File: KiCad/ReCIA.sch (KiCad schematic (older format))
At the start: 1 part, among them U1 8520_DIP

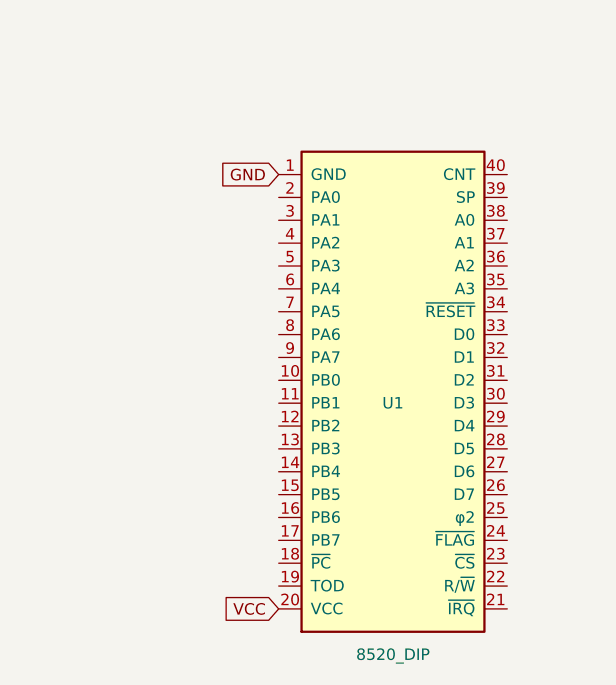
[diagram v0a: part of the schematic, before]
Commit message: Add nets
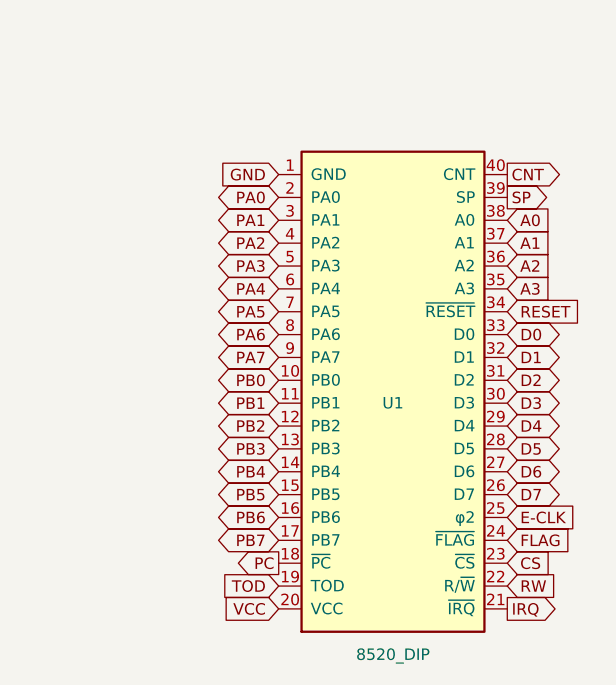
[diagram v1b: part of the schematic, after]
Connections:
- net PB0: now reaches U1.10 (PB0)
- net PB1: now reaches U1.11 (PB1)
- net PB2: now reaches U1.12 (PB2)
- net PB3: now reaches U1.13 (PB3)
- net PB4: now reaches U1.14 (PB4)
- net PB5: now reaches U1.15 (PB5)
- net PB6: now reaches U1.16 (PB6)
- net PB7: now reaches U1.17 (PB7)
- net PC: now reaches U1.18 (~PC)
- net TOD: now reaches U1.19 (TOD)
- net PA0: now reaches U1.2 (PA0)
- net IRQ: now reaches U1.21 (~IRQ)
- net RW: now reaches U1.22 (R/~W)
- net CS: now reaches U1.23 (~CS)
- net FLAG: now reaches U1.24 (~FLAG)
- net E-CLK: now reaches U1.25 (φ2)
- net D7: now reaches U1.26 (D7)
- net D6: now reaches U1.27 (D6)
- net D5: now reaches U1.28 (D5)
- net D4: now reaches U1.29 (D4)
- net PA1: now reaches U1.3 (PA1)
- net D3: now reaches U1.30 (D3)
- net D2: now reaches U1.31 (D2)
- net D1: now reaches U1.32 (D1)
- net D0: now reaches U1.33 (D0)
- net RESET: now reaches U1.34 (~RESET)
- net A3: now reaches U1.35 (A3)
- net A2: now reaches U1.36 (A2)
- net A1: now reaches U1.37 (A1)
- net A0: now reaches U1.38 (A0)
- net SP: now reaches U1.39 (SP)
- net PA2: now reaches U1.4 (PA2)
- net CNT: now reaches U1.40 (CNT)
- net PA3: now reaches U1.5 (PA3)
- net PA4: now reaches U1.6 (PA4)
- net PA5: now reaches U1.7 (PA5)
- net PA6: now reaches U1.8 (PA6)
- net PA7: now reaches U1.9 (PA7)
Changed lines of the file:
@@
 GND
 $Comp
-L power:VCC #PWR?
+L power:VCC #PWR0101
 U 1 1 66BFF4F3
 P 1050 1100
-F 0 "#PWR?" H 1065 1273 50  0001 C CNN
+F 0 "#PWR0101" H 1065 1273 50  0001 C CNN
 F 1 "VCC" H 1065 1273 50  0001 C CNN
 F 2 "" H 1050 1100 50  0001 C CNN
@@
 $EndComp
 $Comp
-L power:PWR_FLAG #FLG?
+L power:PWR_FLAG #FLG0101
 U 1 1 66BFFF76
 P 1050 1200
-F 0 "#FLG?" H 1050 1275 50  0001 C CNN
+F 0 "#FLG0101" H 1050 1275 50  0001 C CNN
 F 1 "PWR_FLAG" H 1050 1373 50  0001 C CNN
 F 2 "" H 1050 1200 50  0001 C CNN
@@
 VCC
 $Comp
-L power:PWR_FLAG #FLG?
+L power:PWR_FLAG #FLG0102
 U 1 1 66C0324F
 P 1200 1100
-F 0 "#FLG?" H 1200 1175 50  0001 C CNN
+F 0 "#FLG0102" H 1200 1175 50  0001 C CNN
 F 1 "PWR_FLAG" H 1200 1273 50  0001 C CNN
 F 2 "" H 1200 1100 50  0001 C CNN
@@
 $EndComp
 $Comp
-L power:GND #PWR?
+L power:GND #PWR0102
 U 1 1 66C03B19
 P 1200 1200
-F 0 "#PWR?" H 1200 950 50  0001 C CNN
+F 0 "#PWR0102" H 1200 950 50  0001 C CNN
 F 1 "GND" H 1205 1027 50  0001 C CNN
 F 2 "" H 1200 1200 50  0001 C CNN
@@
 Wire Wire Line
 	1200 1150 1200 1200
+Text GLabel 2250 2500 0    50   BiDi ~ 0
+PA0
+Text GLabel 2250 2600 0    50   BiDi ~ 0
+PA1
+Text GLabel 2250 2700 0    50   BiDi ~ 0
+PA2
+Text GLabel 2250 2800 0    50   BiDi ~ 0
+PA3
+Text GLabel 2250 2900 0    50   BiDi ~ 0
+PA4
+Text GLabel 2250 3000 0    50   BiDi ~ 0
+PA5
+Text GLabel 2250 3100 0    50   BiDi ~ 0
+PA6
+Text GLabel 2250 3200 0    50   BiDi ~ 0
+PA7
+Text GLabel 2250 3300 0    50   BiDi ~ 0
+PB0
+Text GLabel 2250 3400 0    50   BiDi ~ 0
+PB1
+Text GLabel 2250 3500 0    50   BiDi ~ 0
+PB2
+Text GLabel 2250 3600 0    50   BiDi ~ 0
+PB3
+Text GLabel 2250 3700 0    50   BiDi ~ 0
+PB4
+Text GLabel 2250 3800 0    50   BiDi ~ 0
+PB5
+Text GLabel 2250 3900 0    50   BiDi ~ 0
+PB6
+Text GLabel 2250 4000 0    50   BiDi ~ 0
+PB7
+Text GLabel 3250 2600 2    50   Input ~ 0
+A0
+Text GLabel 3250 2700 2    50   Input ~ 0
+A1
+Text GLabel 3250 2800 2    50   Input ~ 0
+A2
+Text GLabel 3250 2900 2    50   Input ~ 0
+A3
+Text GLabel 3250 3000 2    50   Input ~ 0
+RESET
+Text GLabel 3250 3100 2    50   BiDi ~ 0
+D0
+Text GLabel 3250 3200 2    50   BiDi ~ 0
+D1
+Text GLabel 3250 3300 2    50   BiDi ~ 0
+D2
+Text GLabel 3250 3400 2    50   BiDi ~ 0
+D3
+Text GLabel 3250 3500 2    50   BiDi ~ 0
+D4
+Text GLabel 3250 3600 2    50   BiDi ~ 0
+D5
+Text GLabel 3250 3700 2    50   BiDi ~ 0
+D6
+Text GLabel 3250 3800 2    50   BiDi ~ 0
+D7
+Text GLabel 3250 3900 2    50   Input ~ 0
+E-CLK
+Text GLabel 2250 4100 0    50   Output ~ 0
+PC
+Text GLabel 2250 4200 0    50   Input ~ 0
+TOD
+Text GLabel 3250 4000 2    50   Input ~ 0
+FLAG
+Text GLabel 3250 4100 2    50   Input ~ 0
+CS
+Text GLabel 3250 4200 2    50   Input ~ 0
+RW
+Text GLabel 3250 4300 2    50   Output ~ 0
+IRQ
+Text GLabel 3250 2400 2    50   Output ~ 0
+CNT
+Text GLabel 3250 2500 2    50   Output ~ 0
+SP
 $EndSCHEMATC

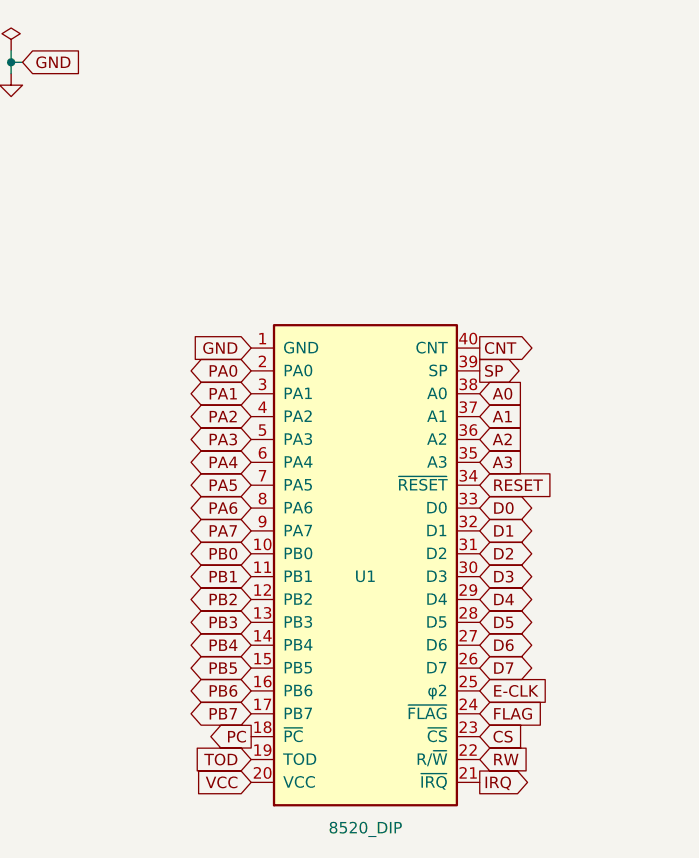
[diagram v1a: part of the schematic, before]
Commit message: Added a 3.3V LDO Voltage Regulator
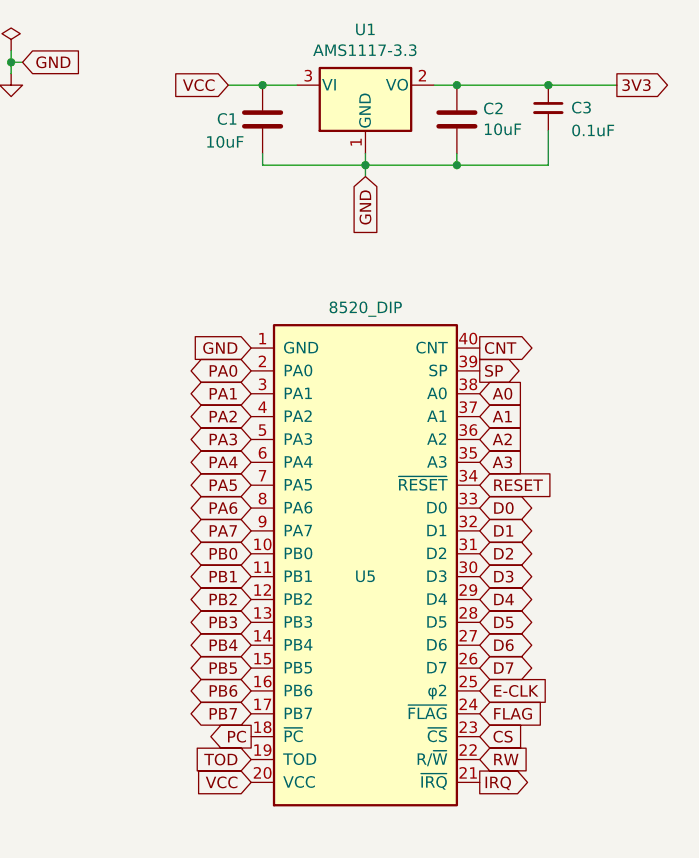
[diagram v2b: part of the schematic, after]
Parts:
- removed U1: 8520_DIP, Package_DIP:DIP-40_W15.24mm, symbol ReCIA:8520_DIP
- added C1, C2: 10uF, Capacitor_SMD:C_1206_3216Metric_Pad1.33x1.80mm_HandSolder, symbol Device:C
- added C3: 0.1uF, Capacitor_SMD:C_0805_2012Metric_Pad1.18x1.45mm_HandSolder, symbol Device:C_Small
- added U1: AMS1117-3.3, Package_TO_SOT_SMD:SOT-223-3_TabPin2, symbol Regulator_Linear:AMS1117-3.3
- added U5: 8520_DIP, Package_DIP:DIP-40_W15.24mm, symbol ReCIA:8520_DIP
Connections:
- net A0: now also U5.38 (A0)
- net A1: now also U5.37 (A1)
- net A2: now also U5.36 (A2)
- net A3: now also U5.35 (A3)
- net CNT: now also U5.40 (CNT)
- net CS: now also U5.23 (~CS)
- net D0: now also U5.33 (D0)
- net D1: now also U5.32 (D1)
- net D2: now also U5.31 (D2)
- net D3: now also U5.30 (D3)
- net D4: now also U5.29 (D4)
- net D5: now also U5.28 (D5)
- net D6: now also U5.27 (D6)
- net D7: now also U5.26 (D7)
- net E-CLK: now also U5.25 (φ2)
- net FLAG: now also U5.24 (~FLAG)
- net GND: now also C1.2, C2.2, C3.2, U1.1 (GND), U5.1 (GND)
- net IRQ: now also U5.21 (~IRQ)
- net PA0: now also U5.2 (PA0)
- net PA1: now also U5.3 (PA1)
- net PA2: now also U5.4 (PA2)
- net PA3: now also U5.5 (PA3)
- net PA4: now also U5.6 (PA4)
- net PA5: now also U5.7 (PA5)
- net PA6: now also U5.8 (PA6)
- net PA7: now also U5.9 (PA7)
- net PB0: now also U5.10 (PB0)
- net PB1: now also U5.11 (PB1)
- net PB2: now also U5.12 (PB2)
- net PB3: now also U5.13 (PB3)
- net PB4: now also U5.14 (PB4)
- net PB5: now also U5.15 (PB5)
- net PB6: now also U5.16 (PB6)
- net PB7: now also U5.17 (PB7)
- net PC: now also U5.18 (~PC)
- net RESET: now also U5.34 (~RESET)
- net RW: now also U5.22 (R/~W)
- net SP: now also U5.39 (SP)
- net TOD: now also U5.19 (TOD)
- net VCC: now also C1.1, U1.3 (VI), U5.20 (VCC)
- new net 3V3: C2.1, C3.1, U1.2 (VO)
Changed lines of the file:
@@
 Comment4 ""
 $EndDescr
-$Comp
-L ReCIA:8520_DIP U1
-U 1 1 66BF3B9F
-P 2750 3400
-F 0 "U1" H 2750 3400 50  0000 C CNN
-F 1 "8520_DIP" H 2750 2300 50  0000 C CNN
-F 2 "Package_DIP:DIP-40_W15.24mm" H 2800 2050 50  0001 L CNN
-F 3 "" H 2750 3400 50  0001 C CNN
-	1    2750 3400
-	1    0    0    -1
-$EndComp
 Text GLabel 2250 2400 0    50   Input ~ 0
 GND
@@
 Text GLabel 3250 2500 2    50   Output ~ 0
 SP
+$Comp
+L ReCIA:8520_DIP U5
+U 1 1 66C0FD06
+P 2750 3400
+F 0 "U5" H 2750 3400 50  0000 C CNN
+F 1 "8520_DIP" H 2750 4576 50  0000 C CNN
+F 2 "Package_DIP:DIP-40_W15.24mm" H 2200 2300 50  0001 L CNN
+F 3 "" H 2750 3200 50  0001 C CNN
+	1    2750 3400
+	1    0    0    -1
+$EndComp
+$Comp
+L Regulator_Linear:AMS1117-3.3 U1
+U 1 1 66C15FFE
+P 2750 1250
+F 0 "U1" H 2750 1492 50  0000 C CNN
+F 1 "AMS1117-3.3" H 2750 1401 50  0000 C CNN
+F 2 "Package_TO_SOT_SMD:SOT-223-3_TabPin2" H 2750 1450 50  0001 C CNN
+F 3 "http://www.advanced-monolithic.com/pdf/ds1117.pdf" H 2850 1000 50  0001 C CNN
+	1    2750 1250
+	1    0    0    -1
+$EndComp
+Text GLabel 2750 1650 3    50   Input ~ 0
+GND
+Text GLabel 2150 1250 0    50   Input ~ 0
+VCC
+Text GLabel 3850 1250 2    50   Output ~ 0
+3V3
+Wire Wire Line
+	2150 1250 2300 1250
+Wire Wire Line
+	3050 1250 3150 1250
+$Comp
+L Device:C C1
+U 1 1 66C1D6E1
+P 2300 1400
+F 0 "C1" H 2100 1400 50  0000 L CNN
+F 1 "10uF" H 2050 1300 50  0000 L CNN
+F 2 "Capacitor_SMD:C_1206_3216Metric_Pad1.33x1.80mm_HandSolder" H 2338 1250 50  0001 C CNN
+F 3 "~" H 2300 1400 50  0001 C CNN
+	1    2300 1400
+	1    0    0    -1
+$EndComp
+Connection ~ 2300 1250
+Wire Wire Line
+	2300 1250 2450 1250
+Wire Wire Line
+	2300 1550 2300 1600
+Wire Wire Line
+	2300 1600 2750 1600
+Wire Wire Line
+	2750 1600 2750 1550
+Wire Wire Line
+	2750 1650 2750 1600
+Connection ~ 2750 1600
+$Comp
+L Device:C C2
+U 1 1 66C1E80A
+P 3150 1400
+F 0 "C2" H 3265 1446 50  0000 L CNN
+F 1 "10uF" H 3265 1355 50  0000 L CNN
+F 2 "Capacitor_SMD:C_1206_3216Metric_Pad1.33x1.80mm_HandSolder" H 3188 1250 50  0001 C CNN
+F 3 "~" H 3150 1400 50  0001 C CNN
+	1    3150 1400
+	1    0    0    -1
+$EndComp
+Connection ~ 3150 1250
+Wire Wire Line
+	2750 1600 3150 1600
+Wire Wire Line
+	3150 1600 3150 1550
+$Comp
+L Device:C_Small C3
+U 1 1 66C24424
+P 3550 1350
+F 0 "C3" H 3650 1350 50  0000 L CNN
+F 1 "0.1uF" H 3650 1250 50  0000 L CNN
+F 2 "Capacitor_SMD:C_0805_2012Metric_Pad1.18x1.45mm_HandSolder" H 3550 1350 50  0001 C CNN
+F 3 "~" H 3550 1350 50  0001 C CNN
+	1    3550 1350
+	1    0    0    -1
+$EndComp
+Wire Wire Line
+	3150 1250 3550 1250
+Wire Wire Line
+	3550 1250 3850 1250
+Connection ~ 3550 1250
+Wire Wire Line
+	3150 1600 3550 1600
+Wire Wire Line
+	3550 1600 3550 1450
+Connection ~ 3150 1600
 $EndSCHEMATC

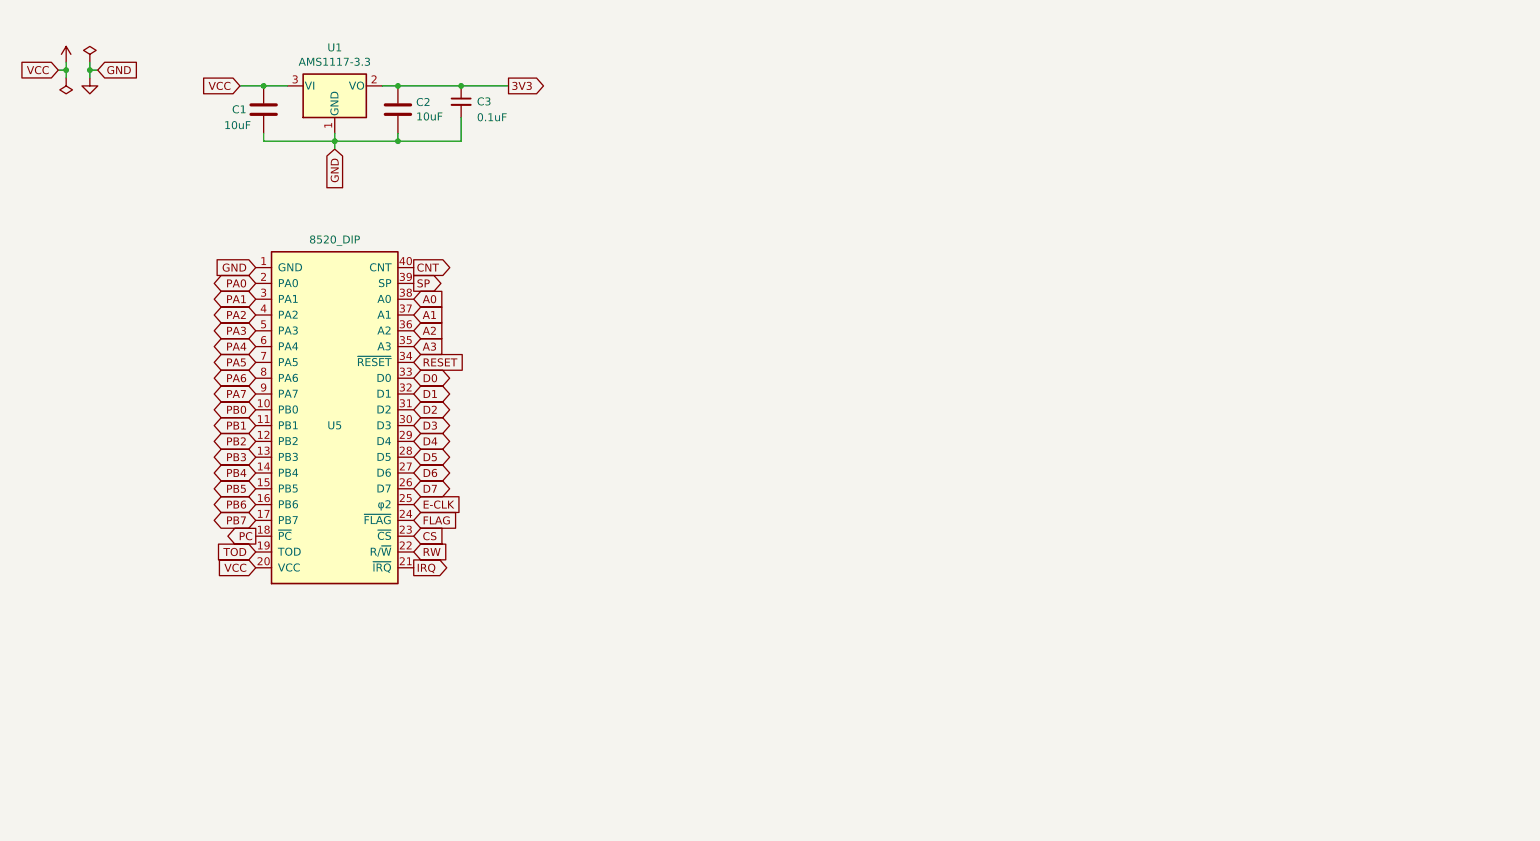
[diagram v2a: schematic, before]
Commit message: Add 10 Max FPGA
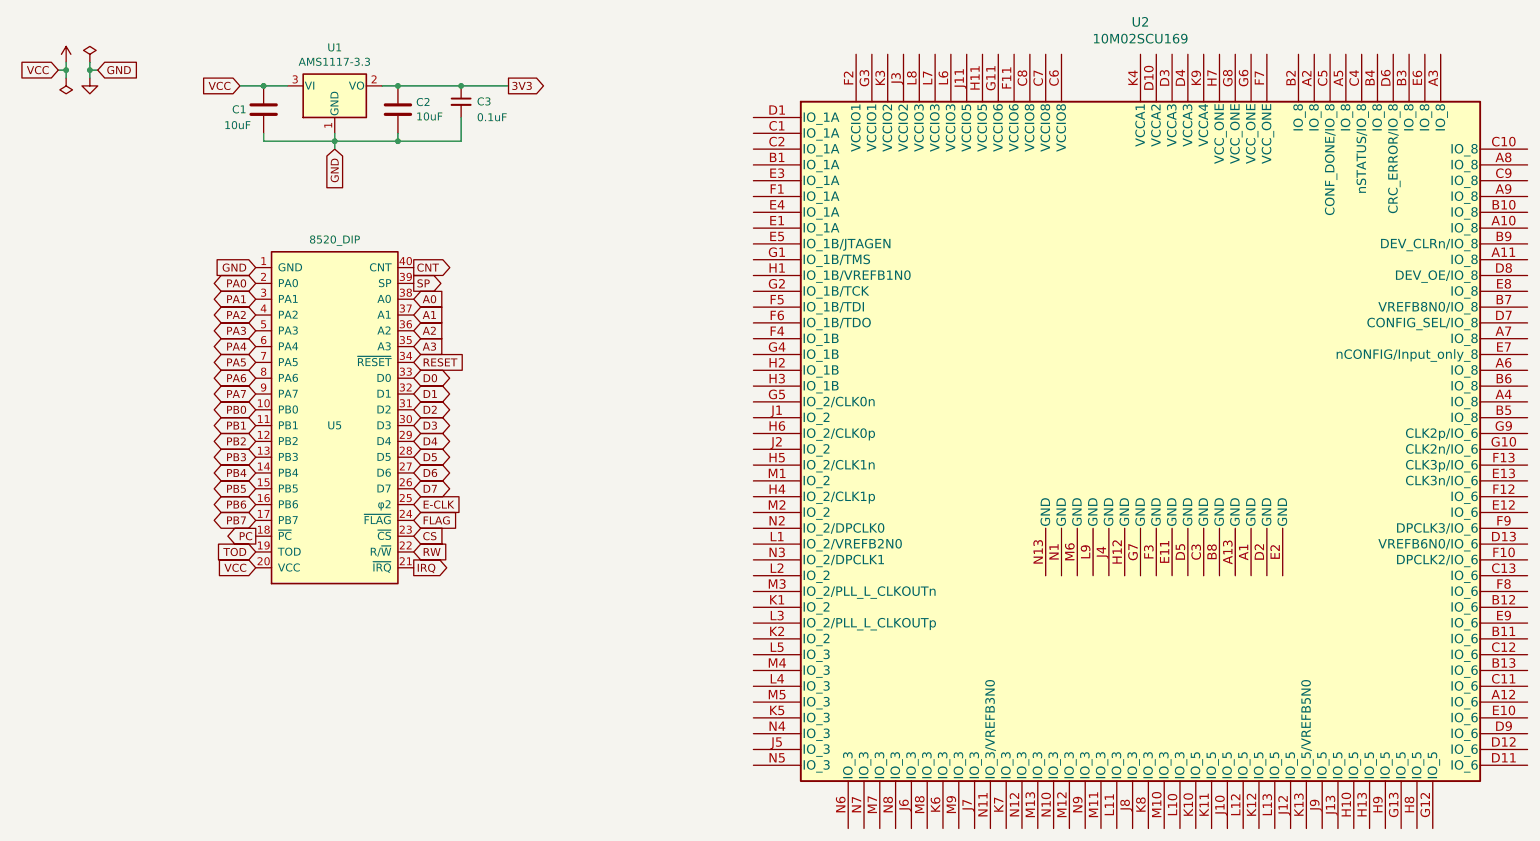
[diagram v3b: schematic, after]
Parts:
- added U2: 10M02SCU169, ReCIA:BGA-169_11.0x11.0mm_Layout13x13_P0.8mm_Ball0.5mm_Pad0.35mm_NSMD, symbol ReCIA:10M02SCU169
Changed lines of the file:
@@
 	3550 1600 3550 1450
 Connection ~ 3150 1600
+$Comp
+L ReCIA:10M02SCU169 U2
+U 1 1 66C35F6F
+P 7850 3500
+F 0 "U2" H 7850 6153 60  0000 C CNN
+F 1 "10M02SCU169" H 7850 6047 60  0000 C CNN
+F 2 "ReCIA:BGA-169_11.0x11.0mm_Layout13x13_P0.8mm_Ball0.5mm_Pad0.35mm_NSMD" H 7850 3850 60  0001 C CNN
+F 3 "" H 9300 4700 60  0000 C CNN
+	1    7850 3500
+	1    0    0    -1
+$EndComp
 $EndSCHEMATC
